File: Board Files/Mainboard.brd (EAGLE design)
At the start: 254 x 94 mm, 115 parts, among them J1 I2C Display

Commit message: Board Layout Update
-Routed VCC and GND to white keys
-Routed GND to black keys
-Placed most components on board
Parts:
- removed R55: 10k, SparkFun-Resistors:AXIAL-0.3
- added R53: 10k, SparkFun-Resistors:AXIAL-0.3
- R10, R12, R14, R16, R18, R2, R20, R22, R24, R4, R49, R6, R8: value (none) -> 10k
- R11, R13, R15, R17, R19, R21, R23, R25, R27, R3, R5, R7, R9: value 10k -> (none)
- VR1: device SparkFun-Resistors:SLIDER-SMALL -> SparkFun-Resistors:POT-PTH-ALPS
- moved D24 383.0 mm to (224.8, 32.4), turned to 180 degrees
- moved D23 363.1 mm to (216.5, 64.8), turned to 180 degrees
- moved R42 362.2 mm to (200.0, 43.2)
- moved D22 354.4 mm to (208.3, 32.4), turned to 180 degrees
- moved R48 348.6 mm to (224.8, 10.2)
- moved S24 348.5 mm to (224.8, 20.3), turned to 180 degrees
- moved R41 346.6 mm to (200.0, 69.8), turned to 180 degrees
- moved R40 344.9 mm to (191.8, 10.2)
- moved D21 334.2 mm to (200.0, 64.8), turned to 180 degrees
- moved R47 330.0 mm to (224.8, 37.5), turned to 180 degrees
- moved S19 329.9 mm to (175.3, 20.3), turned to 180 degrees
- moved R39 326.4 mm to (191.8, 37.5), turned to 180 degrees
- moved D20 326.0 mm to (191.8, 32.4), turned to 180 degrees
- moved S23 320.1 mm to (216.5, 53.3), turned to 180 degrees
- moved B1 312.5 mm to (218.4, 85.1), turned to 270 degrees
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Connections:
- net ENCODER_SWITCH: now also R53.P$1; no longer R55.P$1
- net GND: now also R10.P$2, R12.P$2, R14.P$2, R16.P$2, R18.P$2, R2.P$2, R20.P$2, R22.P$2, R24.P$2, R26.P$2, R4.P$2, R49.P$1, R50.P$1, R6.P$2, R8.P$2, VR1.P$1; no longer R11.P$2, R13.P$2, R15.P$2, R17.P$2, R19.P$2, R21.P$2, R23.P$2, R27.P$2, R3.P$2, R5.P$2, R50.P$2, R51.P$1, R52.P$1, R7.P$2, R9.P$2, VR1.TOP
- net LED1-2: now also R3.P$2; no longer R2.P$2
- net LED1-3: now also R5.P$2; no longer R4.P$2
- net LED1-4: now also R7.P$2; no longer R6.P$2
- net LED1-5: now also R9.P$2; no longer R8.P$2
- net LED1-6: now also R11.P$2; no longer R10.P$2
- net LED1-7: now also R13.P$2; no longer R12.P$2
- net LED1-8: now also R15.P$2; no longer R14.P$2
- net LED2-1: now also R17.P$2; no longer R16.P$2
- net LED2-2: now also R19.P$2; no longer R18.P$2
- net LED2-3: now also R21.P$2; no longer R20.P$2
- net LED2-4: now also R23.P$2; no longer R22.P$2
- net LED2-5: now also R25.P$2; no longer R24.P$2
- net LED2-6: now also R27.P$2; no longer R29.P$2
- net LED2-7: now also R29.P$2; no longer R31.P$2
- net LED2-8: now also R31.P$2; no longer R33.P$2
- net LED3-1: now also R33.P$2; no longer R35.P$2
- net LED3-2: now also R35.P$2; no longer R37.P$2
- net LED3-3: now also R37.P$2; no longer R39.P$2
- net LED3-4: now also R39.P$2; no longer R41.P$2
- net LED3-5: now also R41.P$2; no longer R43.P$2
- net LED3-6: now also R43.P$2; no longer R45.P$2
- net LED3-7: now also R45.P$2; no longer R47.P$2
- net LED3-8: now also R47.P$2; no longer R49.P$2
- net N$10: now also R19.P$1; no longer R18.P$1
- net N$11: now also R21.P$1; no longer R20.P$1
- net N$12: now also R23.P$1; no longer R22.P$1
- net N$13: now also R25.P$1; no longer R24.P$1
- net N$14: now also R27.P$1; no longer R29.P$1
- net N$15: now also R29.P$1; no longer R31.P$1
- net N$16: now also R31.P$1; no longer R33.P$1
- net N$17: now also R33.P$1; no longer R35.P$1
- net N$18: now also R35.P$1; no longer R37.P$1
- net N$19: now also R37.P$1; no longer R39.P$1
- net N$2: now also R3.P$1; no longer R2.P$1
- net N$20: now also R39.P$1; no longer R41.P$1
- net N$21: now also R41.P$1; no longer R43.P$1
- net N$22: now also R43.P$1; no longer R45.P$1
- net N$23: now also R45.P$1; no longer R47.P$1
- net N$24: now also R47.P$1; no longer R49.P$1
- net N$3: now also R5.P$1; no longer R4.P$1
- net N$4: now also R7.P$1; no longer R6.P$1
- net N$5: now also R9.P$1; no longer R8.P$1
- net N$6: now also R11.P$1; no longer R10.P$1
- net N$7: now also R13.P$1; no longer R12.P$1
- net N$8: now also R15.P$1; no longer R14.P$1
- net N$9: now also R17.P$1; no longer R16.P$1
- net OCTAVE_DOWN: now also R50.P$2; no longer R52.P$2
- net OCTAVE_UP: now also R49.P$2; no longer R51.P$2
- net SCL: now also R51.P$1; no longer R25.P$1
- net SDA: now also R52.P$1; no longer R26.P$1
- net SWITCH1-1: now also R2.P$1; no longer R27.P$1
- net SWITCH1-2: now also R4.P$1; no longer R3.P$1
- net SWITCH1-3: now also R6.P$1; no longer R5.P$1
- net SWITCH1-4: now also R8.P$1; no longer R7.P$1
- net SWITCH1-5: now also R10.P$1; no longer R9.P$1
- net SWITCH1-6: now also R12.P$1; no longer R11.P$1
- net SWITCH1-7: now also R14.P$1; no longer R13.P$1
- net SWITCH1-8: now also R16.P$1; no longer R15.P$1
- net SWITCH2-1: now also R18.P$1; no longer R17.P$1
- net SWITCH2-2: now also R20.P$1; no longer R19.P$1
- net SWITCH2-3: now also R22.P$1; no longer R21.P$1
- net SWITCH2-4: now also R24.P$1; no longer R23.P$1
- net SWITCH2-5: now also R26.P$1; no longer R28.P$1
- net SWITCH2-6: now also R28.P$1; no longer R30.P$1
- net SWITCH2-7: now also R30.P$1; no longer R32.P$1
- net SWITCH2-8: now also R32.P$1; no longer R34.P$1
- net SWITCH3-1: now also R34.P$1; no longer R36.P$1
- net SWITCH3-2: now also R36.P$1; no longer R38.P$1
- net SWITCH3-3: now also R38.P$1; no longer R40.P$1
- net SWITCH3-4: now also R40.P$1; no longer R42.P$1
- net SWITCH3-5: now also R42.P$1; no longer R44.P$1
- net SWITCH3-6: now also R44.P$1; no longer R46.P$1
- net SWITCH3-7: now also R46.P$1; no longer R48.P$1
- net SWITCH3-8: now also R48.P$1; no longer R50.P$1
- net VCC: now also R51.P$2, R52.P$2, R53.P$2, VR1.P$3; no longer R25.P$2, R26.P$2, R55.P$2, VR1.BOTTOM
- net VELPOT: now also VR1.P$2; no longer VR1.WIPER
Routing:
- net GND: track 0.00 -> 1359.2 mm
- net VCC: track 0.00 -> 452.3 mm
- net N$20: track 0.00 -> 15.9 mm
- net N$15: track 0.00 -> 15.9 mm
- net N$8: track 0.00 -> 15.9 mm
- net N$12: track 0.00 -> 15.9 mm
- net N$1: track 0.00 -> 15.9 mm
- net N$7: track 0.00 -> 15.9 mm
- net N$3: track 0.00 -> 15.9 mm
- net N$5: track 0.00 -> 15.9 mm
- net N$24: track 0.00 -> 15.9 mm
- net N$22: track 0.00 -> 15.9 mm
- net N$19: track 0.00 -> 15.9 mm
- net N$17: track 0.00 -> 15.9 mm
- net N$13: track 0.00 -> 15.9 mm
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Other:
- board size 254 x 94 mm -> 234.9 x 101.6 mm

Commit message: Routed LEDs and most switches
-Routed all LEDs
-Routes 2/3rds of switches
-Probably need to reroute the right side
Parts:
- moved R52 131.2 mm to (194.3, 92.7), turned to 270 degrees
- moved R51 125.1 mm to (198.1, 92.7), turned to 270 degrees
- moved J1 5.24 mm to (128.3, 94.0)
- moved KEY_REG_3 5.08 mm to (181.6, 87.6), turned to 180 degrees
- moved LED_REG_3 5.08 mm to (181.6, 74.9)
- moved KEY_REG_1 2.54 mm to (72.4, 92.7), turned to 180 degrees
- moved KEY_REG_2 2.54 mm to (95.2, 92.7), turned to 180 degrees
- moved LED_REG_1 2.54 mm to (72.4, 80.0)
- moved LED_REG_2 2.54 mm to (95.2, 80.0)
- moved S28 2.54 mm to (160.0, 88.9)
- moved B1 1.27 mm to (218.4, 83.8)
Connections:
- removed net KEY_CLOCK: KEY_REG_2.10, KEY_REG_3.10
- net REGISTER_CLOCK: now also KEY_REG_2.10, KEY_REG_3.10
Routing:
- net GND: track 1359.2 -> 1.93 mm, vias 0 -> 1
- net VCC: track 452.3 -> 711.3 mm
- net SWITCH1-1: track 5.61 -> 142.6 mm, vias 0 -> 1
- net SWITCH1-3: track 5.61 -> 135.1 mm, vias 0 -> 7
- net SWITCH1-5: track 5.61 -> 113.5 mm, vias 0 -> 5
- net SWITCH1-2: track 5.61 -> 108.2 mm, vias 0 -> 3
- net SWITCH3-8: track 5.61 -> 108.1 mm, vias 0 -> 7
- net LED1-1: track 0.00 -> 97.9 mm
- net SWITCH1-8: track 5.61 -> 103.0 mm, vias 0 -> 3
- net SWITCH3-1: track 5.61 -> 100.2 mm, vias 0 -> 3
- net SWITCH1-7: track 5.61 -> 98.4 mm, vias 0 -> 4
- net SWITCH1-4: track 5.61 -> 93.8 mm, vias 0 -> 3
- net SWITCH3-3: track 5.61 -> 93.6 mm, vias 0 -> 5
- net SWITCH3-4: track 5.61 -> 87.4 mm, vias 0 -> 3
- net SWITCH3-6: track 5.61 -> 84.8 mm, vias 0 -> 5
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- added copper zone on layer 16, net GND
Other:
- board text added: "Bridge J1 Jumper to provide sufficient VCC current/voltage"

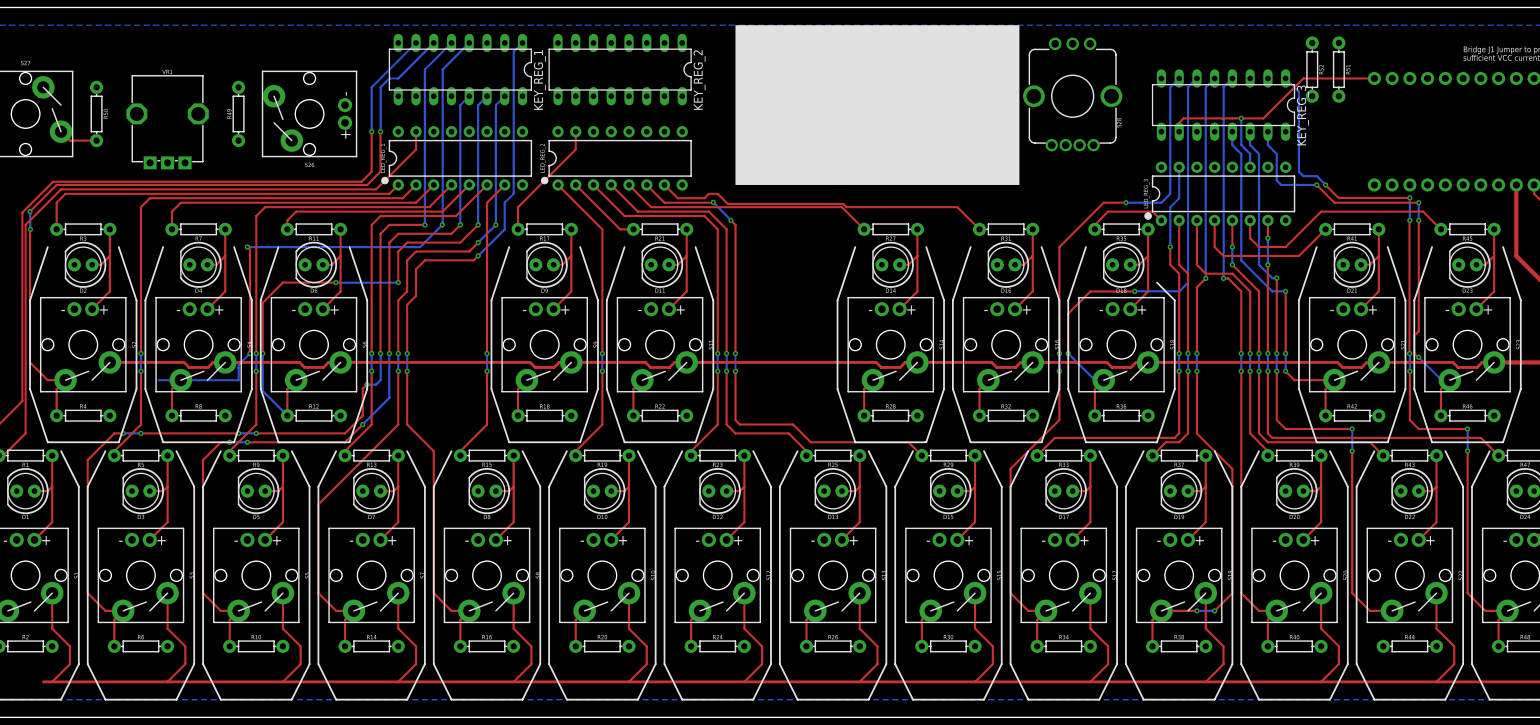
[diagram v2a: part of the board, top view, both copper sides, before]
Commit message: Board Updates, Keycap Updates, Trimmed Libraries
-Finished routing switch and LED traces, will need cleanup
-Made dished versions of keycaps. Thickened top and bottom walls of key stems
-Removed extraneous cherry libraries; fully using Sparkfun and native Eagle ones now
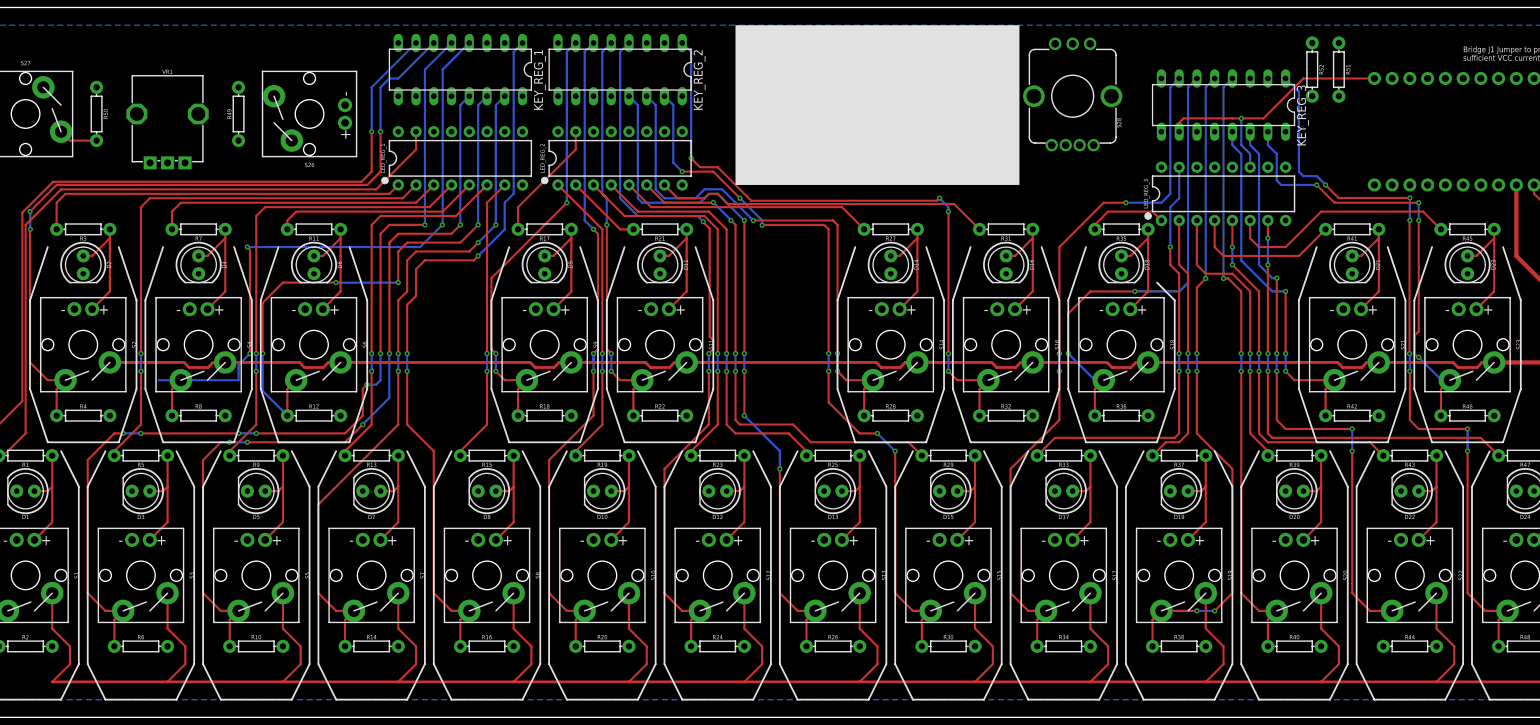
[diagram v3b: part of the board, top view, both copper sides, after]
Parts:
- turned D11 to 270 degrees
- turned D14 to 270 degrees
- turned D16 to 270 degrees
- turned D18 to 270 degrees
- turned D2 to 270 degrees
- turned D21 to 270 degrees
- turned D23 to 270 degrees
- turned D4 to 270 degrees
- turned D6 to 270 degrees
- turned D9 to 270 degrees
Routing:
- net SWITCH2-7: track 5.61 -> 105.9 mm, vias 0 -> 7
- net SWITCH2-4: track 5.61 -> 104.4 mm, vias 0 -> 3
- net SWITCH2-5: track 5.61 -> 99.9 mm, vias 0 -> 5
- net SWITCH2-2: track 5.61 -> 95.4 mm, vias 0 -> 3
- net SWITCH2-8: track 5.61 -> 92.4 mm, vias 0 -> 5
- net SWITCH2-6: track 5.61 -> 75.2 mm, vias 0 -> 3
- net SWITCH2-1: track 5.61 -> 62.8 mm, vias 0 -> 3
- net SWITCH2-3: track 5.61 -> 58.6 mm, vias 0 -> 3
- net N$23: track 15.5 -> 17.3 mm
- net N$18: track 15.5 -> 17.3 mm
- net N$4: track 15.5 -> 17.3 mm
- net N$2: track 15.5 -> 17.3 mm
- net N$11: track 15.5 -> 17.3 mm
- net N$6: track 15.5 -> 17.3 mm
- net N$9: track 15.5 -> 17.3 mm
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
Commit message: Began New PCB
-Deleted cramped PCB, started new layout.
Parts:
- moved R44 350.1 mm to (-119.4, 133.3)
- moved S25 348.5 mm to (-114.3, 114.3), turned to 0 degrees
- moved D24 334.4 mm to (-99.1, 115.6), turned to 0 degrees
- moved R43 331.7 mm to (-109.2, 133.3), turned to 0 degrees
- moved S24 317.8 mm to (-87.6, 78.7), turned to 0 degrees
- moved D23 313.4 mm to (-92.7, 115.6), turned to 0 degrees
- moved R42 312.4 mm to (-99.1, 133.3)
- moved D22 306.2 mm to (-86.4, 115.6), turned to 0 degrees
- moved R48 301.1 mm to (-48.3, 137.2)
- moved S19 298.9 mm to (-120.7, 62.2), turned to 0 degrees
- moved R40 297.2 mm to (-78.7, 133.3)
- moved R41 295.8 mm to (-88.9, 133.3), turned to 0 degrees
- moved R33 293.0 mm to (-119.4, 129.5), turned to 0 degrees
- moved S23 288.8 mm to (-71.1, 78.7), turned to 0 degrees
- moved R52 286.7 mm to (-88.9, 137.2), turned to 0 degrees
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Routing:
- net VCC: track 710.0 -> 0.00 mm
- net SWITCH1-1: track 142.6 -> 0.00 mm, vias 1 -> 0
- net SWITCH1-3: track 135.1 -> 0.00 mm, vias 7 -> 0
- net SWITCH1-5: track 113.5 -> 0.00 mm, vias 5 -> 0
- net SWITCH1-2: track 108.2 -> 0.00 mm, vias 3 -> 0
- net SWITCH3-8: track 108.1 -> 0.00 mm, vias 7 -> 0
- net SWITCH2-7: track 105.9 -> 0.00 mm, vias 7 -> 0
- net SWITCH2-4: track 104.4 -> 0.00 mm, vias 3 -> 0
- net SWITCH1-8: track 103.0 -> 0.00 mm, vias 3 -> 0
- net SWITCH3-1: track 100.2 -> 0.00 mm, vias 3 -> 0
- net SWITCH2-5: track 99.9 -> 0.00 mm, vias 5 -> 0
- net SWITCH1-7: track 98.4 -> 0.00 mm, vias 4 -> 0
- net LED1-1: track 97.9 -> 0.00 mm
- net SWITCH2-2: track 95.4 -> 0.00 mm, vias 3 -> 0
- net SWITCH1-4: track 93.8 -> 0.00 mm, vias 3 -> 0
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- removed copper zone on layer 16, net GND
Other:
- board outline removed
- board text removed: "Bridge J1 Jumper to provide sufficient VCC current/voltage"

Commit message: Updated BRD and SCH
-Added more smoothing caps to schematic, placed things, reverted to old STL files
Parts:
- added C2, C3: 10uF, SparkFun-Capacitors:CPOL-RADIAL-2.5MM-5MM
- moved R44 398.7 mm to (256.5, 0.64)
- moved S25 398.4 mm to (279.4, 53.3), turned to 270 degrees
- moved D24 386.4 mm to (275.6, 21.0), turned to 270 degrees
- moved R43 381.4 mm to (256.5, 25.4)
- moved S24 369.6 mm to (275.6, 10.2), turned to 180 degrees
- moved D23 363.8 mm to (266.1, 55.2), turned to 270 degrees
- moved R42 359.8 mm to (247.0, 34.9)
- moved D22 355.7 mm to (256.5, 21.0), turned to 270 degrees
- moved R48 351.5 mm to (275.6, 0.64)
- moved R41 343.9 mm to (247.0, 59.7)
- moved S19 343.1 mm to (218.4, 10.2), turned to 180 degrees
- moved R40 342.9 mm to (237.5, 0.64)
- moved S23 338.9 mm to (266.1, 44.5), turned to 180 degrees
- moved R33 336.0 mm to (200.0, 25.4)
- moved R47 333.0 mm to (275.6, 25.4)
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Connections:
- net GND: now also C2.2, C3.2
- net VCC: now also C2.1, C3.1
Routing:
- net VCC: track 0.00 -> 567.8 mm
- net RESET: track 0.00 -> 14.2 mm
- net N$24: track 0.00 -> 12.6 mm
- net N$22: track 0.00 -> 12.6 mm
- net N$5: track 0.00 -> 12.6 mm
- net N$19: track 0.00 -> 12.6 mm
- net N$15: track 0.00 -> 12.6 mm
- net N$13: track 0.00 -> 12.6 mm
- net N$18: track 0.00 -> 12.6 mm
- net N$14: track 0.00 -> 12.6 mm
- net N$11: track 0.00 -> 12.6 mm
- net N$1: track 0.00 -> 12.6 mm
- net N$8: track 0.00 -> 12.6 mm
- net N$7: track 0.00 -> 12.6 mm
- net N$3: track 0.00 -> 12.6 mm
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- added copper zone on layer 16, net GND

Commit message: Finished Manual Routing
Finished routing manual traces. Will autoroute the switch and LED traces
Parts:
- added R54, R55: (no value), SparkFun-Resistors:AXIAL-0.3
- moved KEY_REG_3 284.0 mm to (234.9, 81.3)
- moved LED_REG_3 284.0 mm to (234.9, 69.8)
- moved C3 282.1 mm to (219.7, 81.3)
- moved J1 236.8 mm to (105.8, 87.7)
- moved KEY_REG_2 227.4 mm to (204.5, 81.3)
- moved LED_REG_2 227.4 mm to (204.5, 69.8)
- moved C2 224.0 mm to (189.2, 81.3)
- moved S28 195.3 mm to (143.5, 77.5)
- moved S26 184.2 mm to (80.0, 77.5)
- moved KEY_REG_1 163.7 mm to (174.0, 81.3)
- moved LED_REG_1 163.7 mm to (174.0, 69.8)
- moved C1 162.7 mm to (158.8, 81.3)
- moved S27 154.9 mm to (34.3, 77.5)
- moved VR1 149.4 mm to (57.1, 77.5), turned to 270 degrees
- moved R50 107.4 mm to (44.5, 78.7), turned to 90 degrees
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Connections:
- removed net LED_ENABLE: LED_REG_1.13, LED_REG_2.13, LED_REG_3.13
- new net N$25: R54.P$2, S28.+G
- new net N$26: R55.P$2, S28.+R
- net ENCODER_GREEN: now also R54.P$1; no longer S28.+G
- net ENCODER_RED: now also R55.P$1; no longer S28.+R
- net LED_OUTPUT_EN: now also LED_REG_1.13, LED_REG_2.13, LED_REG_3.13
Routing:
- net VCC: track 567.8 -> 1018.5 mm, vias 0 -> 3
- net GND: track 1.93 -> 340.7 mm, vias 1 -> 5
- net OCTAVE_DOWN: track 0.00 -> 227.1 mm
- net VELPOT: track 0.00 -> 198.7 mm
- net OCTAVE_UP: track 0.00 -> 183.9 mm
- net SCL: track 0.00 -> 168.6 mm
- net SDA: track 0.00 -> 167.0 mm
- net REGISTER_CLOCK: track 0.00 -> 164.3 mm, vias 0 -> 1
- net ENCODER_SWITCH: track 0.00 -> 150.0 mm
- net ENCODER_GREEN: track 0.00 -> 124.1 mm, vias 0 -> 3
- net ENCODER_DIGITAL: track 0.00 -> 123.4 mm, vias 0 -> 1
- net ENCODER_ANALOG: track 0.00 -> 118.8 mm, vias 0 -> 1
- net ENCODER_RED: track 0.00 -> 115.7 mm, vias 0 -> 1
- net LED_DATA: track 0.00 -> 103.4 mm, vias 0 -> 1
- net LED_LATCH: track 0.00 -> 99.7 mm, vias 0 -> 3
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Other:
- board outline added: 268 x 101.6 mm

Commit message: Preliminary Finished Layout
WIth help of autorouter and hand finishing, completed an initial PCB layout
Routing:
- net SWITCH1-7: track 4.97 -> 302.1 mm, vias 0 -> 1
- net SWITCH3-1: track 4.97 -> 228.9 mm, vias 0 -> 1
- net LED1-1: track 0.00 -> 221.6 mm, vias 0 -> 2
- net SWITCH1-1: track 5.61 -> 225.3 mm, vias 0 -> 4
- net SWITCH1-3: track 5.61 -> 211.6 mm, vias 0 -> 4
- net SWITCH1-2: track 4.97 -> 192.1 mm, vias 0 -> 5
- net SWITCH1-5: track 4.97 -> 179.7 mm, vias 0 -> 2
- net SWITCH3-6: track 4.97 -> 171.3 mm, vias 0 -> 1
- net SWITCH2-2: track 4.97 -> 166.4 mm, vias 0 -> 5
- net SWITCH3-8: track 4.97 -> 152.5 mm, vias 0 -> 3
- net SWITCH2-1: track 4.97 -> 151.3 mm, vias 0 -> 1
- net LED1-3: track 0.00 -> 145.7 mm, vias 0 -> 3
- net SWITCH1-4: track 4.97 -> 146.7 mm, vias 0 -> 2
- net LED1-5: track 0.00 -> 137.7 mm, vias 0 -> 3
- net SWITCH2-4: track 4.97 -> 141.4 mm, vias 0 -> 2
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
